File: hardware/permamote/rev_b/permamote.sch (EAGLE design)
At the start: 130 parts, among them J1 TC2030-JLINK-L, J2 M10X2, J3 M04X2, Q1 PMDXB950UPEL, Q10 CSD22206W, Q11 CSD22206W, Q2 PMDXB950UPEL, Q3 PMDXB950UPEL, Q4 PMDXB950UPEL, Q5 PMDXB950UPEL, Q6 PMDXB950UPEL, Q7 CSD22206W, Q8 CSD22206W, Q9 CSD22206W, U1 AB1815-T3, U10 NRF52840, U11 SI7021-A20-GM1, U2 BQ25505, U3 EKMB1101111, U4 ISL29125, U5 LIS2DW12, U6 MAX17222, U7 MAX44009, U8 MS5637-02BA03, U9 NRF51822QF, X1 32MHz, X2 ABS05-32.768KHZ-9-T, X3 32.768kHz, X4 ABS07-32.768KHZ-7-T, X5 16MHz

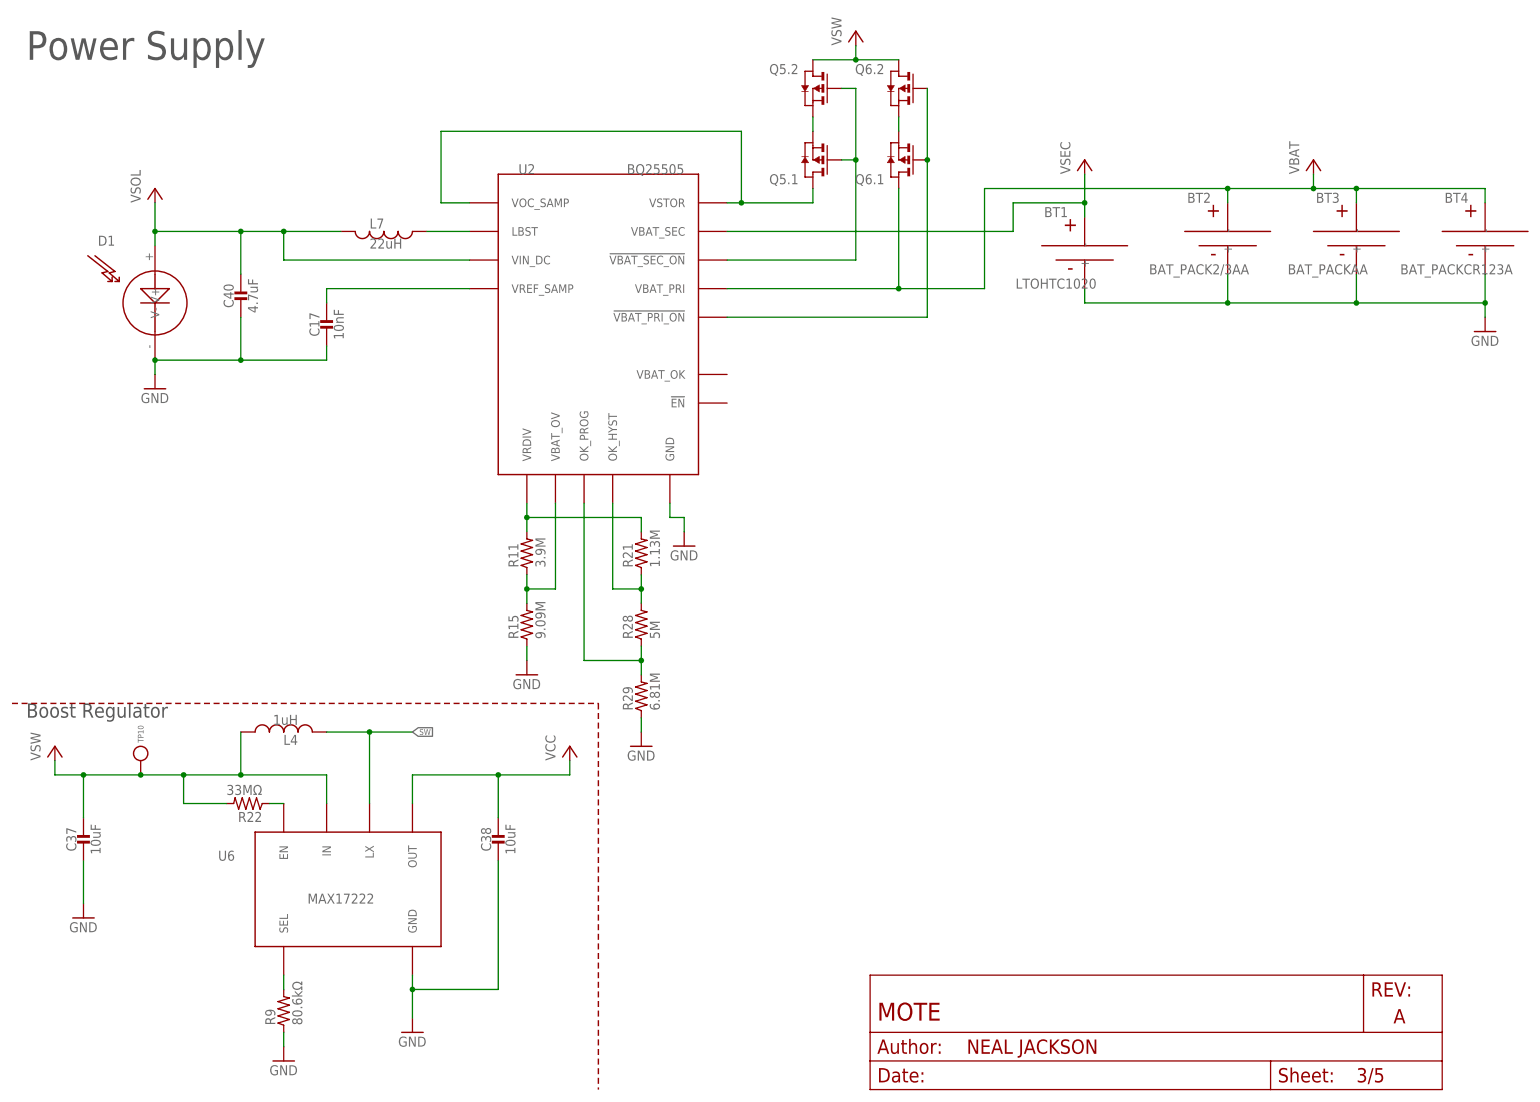
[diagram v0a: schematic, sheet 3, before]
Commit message: fixed bq dividers, changed inductor
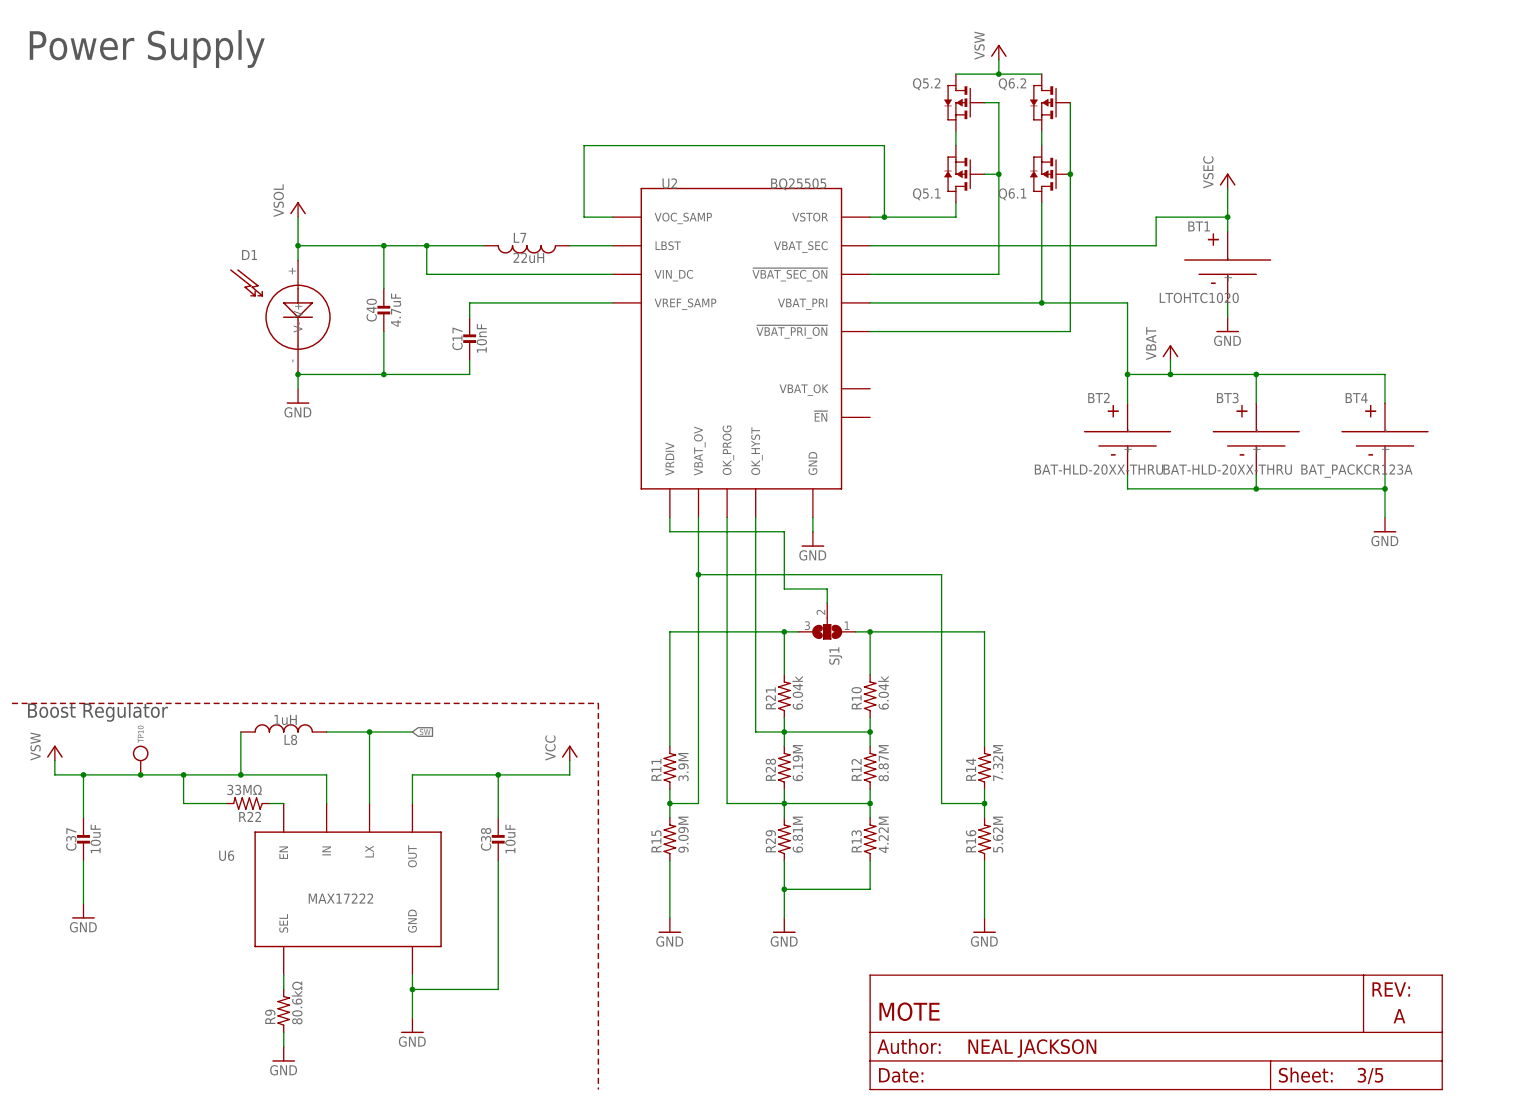
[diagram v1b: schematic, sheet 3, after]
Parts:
- removed L4: 1uH, passives:INDUCTORIHL2525CZ
- added L8: 1uH, passives:INDUCTORIHL
- added R10: 6.04k, passives:RESISTOR0402_RES
- added R12: 8.87M, passives:RESISTOR0402_RES
- added R13: 4.22M, passives:RESISTOR0402_RES
- added R14: 7.32M, passives:RESISTOR0402_RES
- added R16: 5.62M, passives:RESISTOR0402_RES
- added SJ1: (no value), jumper:SJ2W
- BT2: value BAT_PACK2/3AA -> BAT-HLD-20XX-THRU; device batteries:BAT_PACK2/3AA -> batteries:BAT-HLD-20XX-THRU
- BT3: value BAT_PACKAA -> BAT-HLD-20XX-THRU; device batteries:BAT_PACKAA -> batteries:BAT-HLD-20XX-THRU
- R21: value 1.13M -> 6.04k
- R28: value 5M -> 6.19M
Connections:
- new net N$1: R11.2, R21.2, SJ1.3
- new net N$16: R10.2, R14.2, SJ1.1
- net GND: now also R13.1, R16.1
- net N$18: now also R14.1, R16.2
- net N$32: now also SJ1.2; no longer R11.2, R21.2
- net N$57: now also R12.1, R13.2
- net N$58: now also R10.1, R12.2
- net SW: now also L8.2; no longer L4.2
- net VSW: now also L8.1; no longer L4.1
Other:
- note added: "Divider for Lithium Polymer"
- note added: "Divider for Lithium Titanate"
- moved on the sheet: BT1, BT2, BT3, BT4, C17, C40, D1, L7, Q5.1, Q5.2, Q6.1, Q6.2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

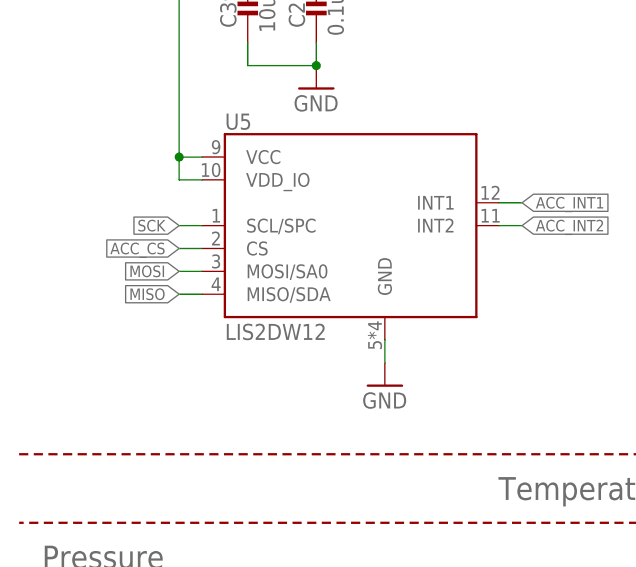
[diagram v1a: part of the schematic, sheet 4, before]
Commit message: Fix miso/mosi switch
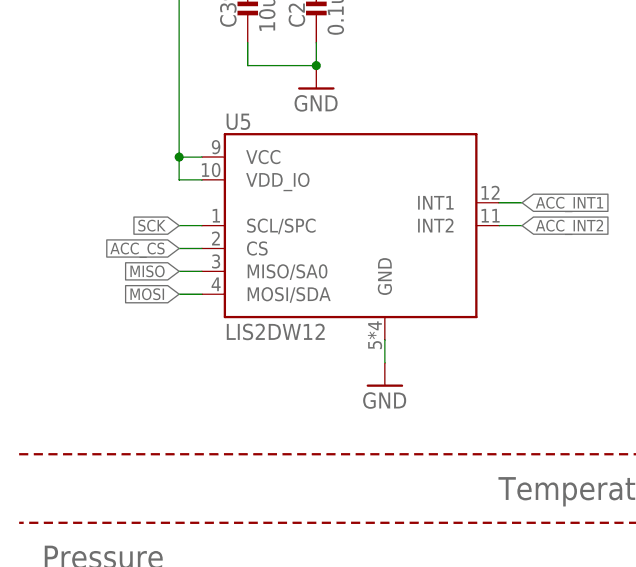
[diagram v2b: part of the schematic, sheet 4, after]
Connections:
- net MISO: now also U5.MISO/SA0; no longer U5.MISO/SDA
- net MOSI: now also U5.MOSI/SDA; no longer U5.MOSI/SA0
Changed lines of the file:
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@@
 <?xml version="1.0" encoding="utf-8"?>
 <!DOCTYPE eagle SYSTEM "eagle.dtd">
-<eagle version="8.4.1">
+<eagle version="8.4.2">
 <drawing>
 <settings>
@@
 <setting verticaltext="up"/>
 </settings>
-<grid distance="0.1" unitdist="inch" unit="inch" style="lines" multiple="1" display="yes" altdistance="0.05" altunitdist="inch" altunit="inch"/>
+<grid distance="0.1" unitdist="inch" unit="inch" style="lines" multiple="1" display="no" altdistance="0.01" altunitdist="inch" altunit="inch"/>
 <layers>
 <layer number="1" name="Top" color="4" fill="1" visible="no" active="no"/>
@@
 <segment>
 <pinref part="U2" gate="G$1" pin="VRDIV"/>
-<wire x1="116.84" y1="101.6" x2="116.84" y2="99.06" width="0.1524" layer="91"/>
-<wire x1="137.16" y1="99.06" x2="116.84" y2="99.06" width="0.1524" layer="91"/>
-<wire x1="137.16" y1="99.06" x2="137.16" y2="88.9" width="0.1524" layer="91"/>
-<wire x1="137.16" y1="88.9" x2="144.78" y2="88.9" width="0.1524" layer="91"/>
+<wire x1="116.84" y1="88.9" x2="116.84" y2="101.6" width="0.1524" layer="91"/>
+<wire x1="116.84" y1="88.9" x2="144.78" y2="88.9" width="0.1524" layer="91"/>
 <pinref part="SJ1" gate="G$1" pin="2"/>
 <wire x1="144.78" y1="88.9" x2="144.78" y2="86.36" width="0.1524" layer="91"/>
@@
 </segment>
 </net>
-<net name="MOSI" class="0">
-<segment>
-<pinref part="U5" gate="G$1" pin="MOSI/SA0"/>
-<wire x1="20.32" y1="109.22" x2="17.78" y2="109.22" width="0.1524" layer="91"/>
-<label x="17.78" y="109.22" size="1.27" layer="95" rot="R180" xref="yes"/>
-</segment>
-</net>
-<net name="MISO" class="0">
-<segment>
-<pinref part="U5" gate="G$1" pin="MISO/SDA"/>
-<wire x1="20.32" y1="106.68" x2="17.78" y2="106.68" width="0.1524" layer="91"/>
-<label x="17.78" y="106.68" size="1.27" layer="95" rot="R180" xref="yes"/>
-</segment>
-</net>
 <net name="ACC_INT1" class="0">
 <segment>
@@
 </segment>
 </net>
+<net name="MISO" class="0">
+<segment>
+<pinref part="U5" gate="G$1" pin="MISO/SA0"/>
+<wire x1="20.32" y1="109.22" x2="17.78" y2="109.22" width="0.1524" layer="91"/>
+<label x="17.78" y="109.22" size="1.27" layer="95" rot="R180" xref="yes"/>
+</segment>
+</net>
+<net name="MOSI" class="0">
+<segment>
+<pinref part="U5" gate="G$1" pin="MOSI/SDA"/>
+<wire x1="20.32" y1="106.68" x2="17.78" y2="106.68" width="0.1524" layer="91"/>
+<label x="17.78" y="106.68" size="1.27" layer="95" rot="R180" xref="yes"/>
+</segment>
+</net>

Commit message: WIP rev_b
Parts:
- removed A1: ANT3216A063R2400A, chips:ANT3216A063R2400A
- removed B2: BAL-NRF01D3, chips:BAL-NRF01D3
- removed C14, C15: 1nF, passives:CAPACITOR0402_CAP
- removed C16: 2.2nF, passives:CAPACITOR0402_CAP
- removed C19: 47nF, passives:CAPACITOR0402_CAP
- removed C28: 0.1uF, passives:CAPACITOR0402_CAP
- removed C3: 0.8pF, passives:CAPACITOR0402_CAP
- removed C34: 1uF, passives:CAPACITOR0402_CAP
- removed C36: 4.7uF, passives:CAPACITOR0402_CAP
- removed C6, C7, C8, C9: 12pF, passives:CAPACITOR0402_CAP
- removed H1, H2, H3, H4: MOUNT-PAD-ROUND3.0, holes:MOUNT-PAD-ROUND3.0
- removed JP1, JP2, JP3, JP4, JP5, JP6, JP7, JP8: (no value), SparkFun-Passives:JUMPER-2SMD-NC
- removed JP10, JP11, JP12, JP13, JP14, JP15, JP16, JP9: (no value), SparkFun-Connectors:M02PTH
- removed L2: 15nH, passives:INDUCTOR0402
- removed L5: 10uH, passives:INDUCTOR0603
- removed Q11, Q9: CSD22206W, fets:CSD22206W
- removed R8: 12kΩ, passives:RESISTOR0402_RES
- removed TP10: TEST_POINT_0.040IN, headers:TEST_POINT_0.040IN
- removed U9: NRF51822QF, chips:NRF51822QF
- removed X2: ABS05-32.768KHZ-9-T, crystals:ABS05-32.768KHZ-9-T
- removed X5: 16MHz, crystals:TXC-8Y
- added C41: 0.1uF, passives:CAPACITOR0402_CAP
- added J5: MICRO_USB_B_HIROSE_ZX62R-B-5P, connector:MICRO_USB_B_HIROSE_ZX62R-B-5P
- added U12: FT232RQ, ftdichip:FT232RQ
- J1: value TC2030-JLINK-L -> TC2030-JLINK-NL; device connector:TC2030-JLINK-L -> connector:TC2030-JLINK-NL
- Q10, Q7, Q8: value CSD22206W -> PMDXB950UPEL; device fets:CSD22206W -> fets:PMDXB950UPEL
- R1: value 150Ω -> 10kΩ; DIGIKEY 311-150JRCT-ND -> 311-10KJRCT-ND
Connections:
- removed net AVDD1: C14.1, C34.1, L2.1, U9.AVDD
- removed net DCC1: L5.2, U9.DCC
- removed net N$15: C25.1, C39.1, JP1.1, JP11.1, U5.VCC, U5.VDD_IO
- removed net N$19: C26.1, JP15.1, JP4.1, Q9.S, R25.2
- removed net N$24: JP14.1, JP8.1, Q11.S, R27.2
- removed net N$33: C24.1, C31.1, JP12.1, JP2.1, Q7.S, R23.2, R4.2
- removed net N$36: C27.1, JP16.1, JP5.1, Q10.S, R26.2
- removed net N$37: C32.1, JP13.1, JP3.1, Q8.S, R24.2, R5.2
- removed net N$42: C33.1, JP10.1, JP6.1, U1.VCC
- removed net N$60: B2.ANT1, U9.ANT1
- removed net N$61: B2.ANT2, U9.ANT2
- removed net N$62: A1.ANTENNA, B2.SE, C3.1
- removed net N$63: L2.2, L5.1
- removed net N$64: C6.1, U9.XC1, X5.1
- removed net N$65: C7.1, U9.XC2, X5.2
- removed net N$66: C15.1, U9.DEC1
- removed net N$67: C19.1, U9.DEC2
- removed net NRF_A2: C9.1, U9.P27/AIN1/XL1, X2.2
- removed net NRF_A3: C8.1, U9.P26/AIN0/XL2, X2.1
- removed net VCC_JUMP: C20.1, C21.1, C23.1, C28.1, C29.1, C35.1, C36.1, JP7.1, JP9.1, U10.VDD, U10.VDDH, U9.VDD
- removed net VDD_PA1: B2.VDD_PA, C16.1, U9.VDD_PA
- new net D+: J5.D+, U12.USBDP
- new net D-: J5.D-, U12.USBDM
- new net DBG_RX: U12.TXD
- new net DBG_TX: U12.RXD
- new net N$13: C41.1, U12.3V3OUT
- new net USB_5V: J5.+5V, U12.VCC
- net !ACC_EN: no longer U10.P1.15, U9.P16
- net !CLR_EN: now also Q7.1.G; no longer Q7.G, U9.P17
- net !CLR_INT: no longer U9.P29
- net !HUM_EN: now also Q8.2.G; no longer Q10.G, U9.P15
- net !LT_EN: now also Q7.2.G; no longer Q8.G, U9.P18
- net !LT_INT: no longer U9.P28
- net !PIR_EN: now also Q10.1.G; no longer Q11.G, U9.P19
- net !PR_EN: now also Q8.1.G; no longer Q9.G, U9.P20
- net !RST: now also U12.!RESET; no longer R1.1
- net !RTC_IRQ1: no longer U9.P25
- net !RTC_IRQ2: no longer U9.P24
- net !RTC_IRQ3: no longer U9.P23
- net ACC_CS: no longer U9.P14
- net ACC_INT1: no longer U9.P06/AIN7/AREF1
- net ACC_INT2: no longer U9.P07
- net GND: now also C41.2, J5.GND, U12.GND, U12.GND@1, U12.GND@2, U12.GND@A, U12.TEST; no longer A1.GND, B2.GND, C14.2, C15.2, C16.2, C19.2, C28.2, C3.2, C34.2, C36.2, C6.2, C7.2, C8.2, C9.2, H1.MOUNT, H2.MOUNT, H3.MOUNT, H4.MOUNT, R8.2, U9.GND
- net MISO: no longer U9.P11
- net MOSI: no longer U9.P12
- net N$20: now also Q7.2.D; no longer Q8.D
- net N$21: now also Q8.1.D; no longer Q9.D
- net N$22: now also Q8.2.D; no longer Q10.D
- net N$23: now also Q10.1.D; no longer Q11.D
- net N$31: now also Q7.1.D; no longer Q7.D
- net PIR_OUT: no longer U9.P30
- net RTC_CS: no longer U9.P22
- net SCK: no longer U9.P13
- net SCL: no longer U9.P10
- net SDA: no longer U9.P08
- net SW: no longer U9.P04/AIN5
- net SWDCLK: no longer R8.1, U9.SWDCLK
- net SWDIO: no longer J1.SWO, R1.2, U9.SWDIO/!RESET
- net VBAT: now also U1.VBAT; no longer JP10.2, JP6.2, R6.2, R7.2, U9.P02/AIN3
- net VCC: now also C20.1, C21.1, C23.1, C24.1, C25.1, C26.1, C27.1, C29.1, C31.1, C32.1, C33.1, C35.1, C39.1, Q10.1.S, Q7.1.S, Q7.2.S, Q8.1.S, Q8.2.S, R1.2, R23.2, R24.2, R25.2, R26.2, R27.2, R4.2, R5.2, R6.2, R7.2, U1.VCC, U10.VDD, U10.VDDH, U12.VCCIO, U5.VCC, U5.VDD_IO; no longer JP1.2, JP11.2, JP12.2, JP13.2, JP14.2, JP15.2, JP16.2, JP2.2, JP3.2, JP4.2, JP5.2, JP7.2, JP8.2, JP9.2
- net VSEC: no longer U9.P01/AIN2
- net VSOL: no longer U9.P03/AIN4
- net VSW: no longer TP10.TESTPOINT
- net WDI: now also R1.1; no longer U9.P21
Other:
- note added: "Debugging"
- note removed: "Auxillary NRF51822"
- note removed: "Mounting Holes"

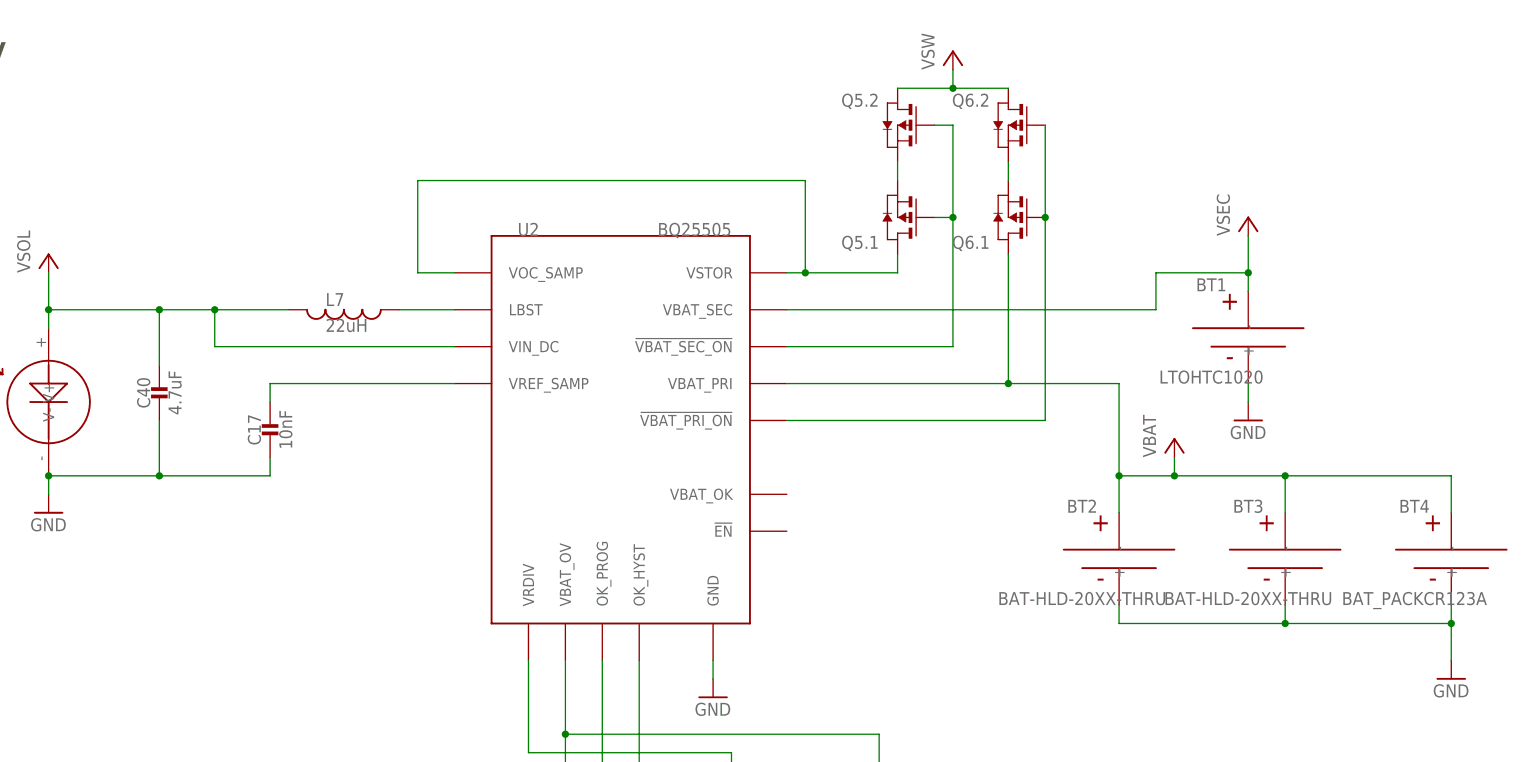
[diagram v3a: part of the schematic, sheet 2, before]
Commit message: WIP
Finish power routing
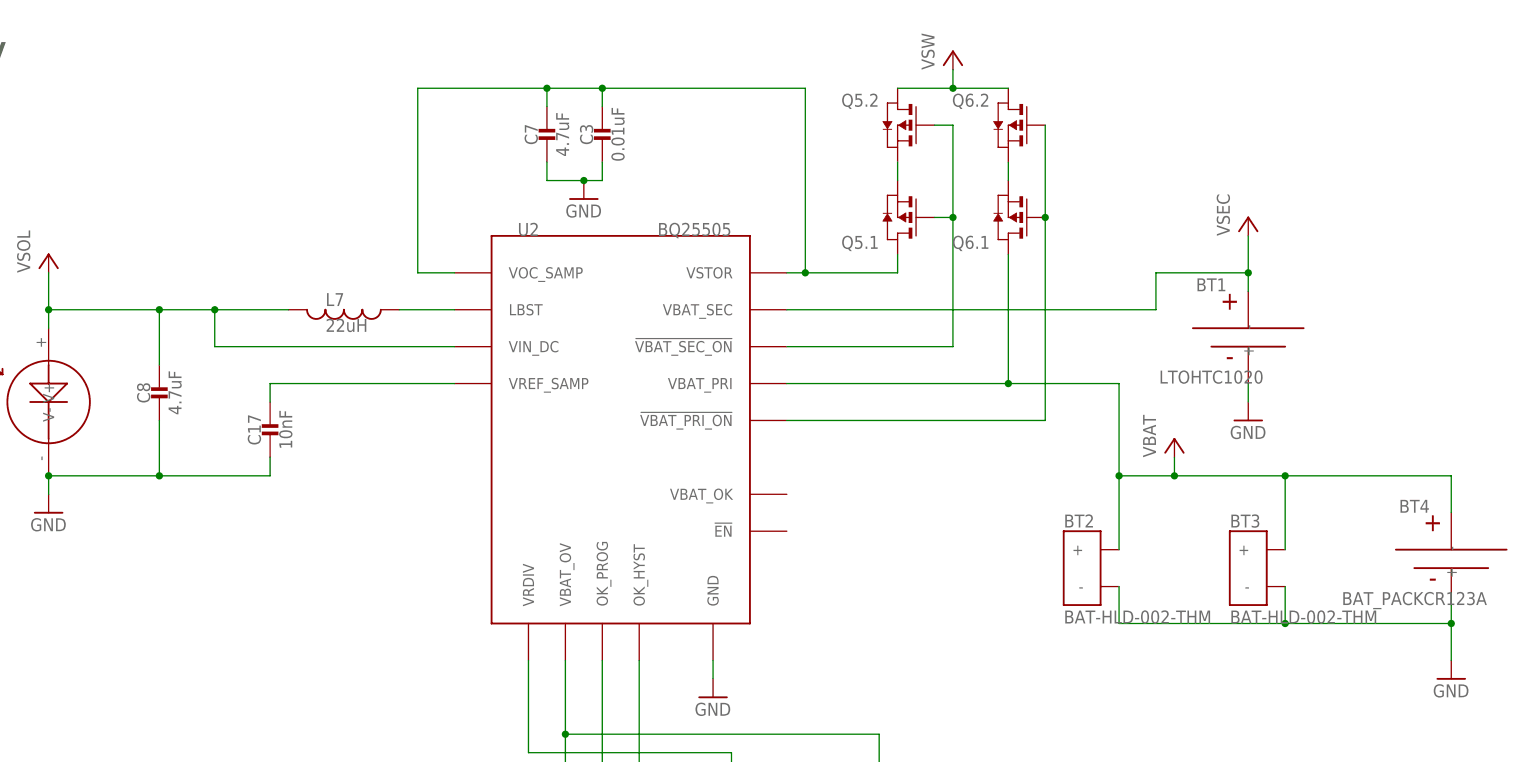
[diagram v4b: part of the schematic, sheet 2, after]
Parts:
- removed C40: 4.7uF, passives:CAPACITOR0603_CAP
- added C3: 0.01uF, passives:CAPACITOR0402_CAP
- added C7, C8: 4.7uF, passives:CAPACITOR0402_CAP
- BT2, BT3: value BAT-HLD-20XX-THRU -> BAT-HLD-002-THM; device batteries:BAT-HLD-20XX-THRU -> batteries:BAT-HLD-002-THM
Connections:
- net N$30 renamed VREF_SAMP
- net N$40 renamed LBST
- net N$46 renamed !VBAT_SEC_ON
- net N$56 renamed !VBAT_PRI_ON
- removed net N$47: Q5.1.D, U2.VOC_SAMP, U2.VSTOR
- new net VOC_SAMP_VSTOR: C3.1, C7.1, Q5.1.D, U2.VOC_SAMP, U2.VSTOR
- net GND: now also C3.2, C7.2, C8.2; no longer C40.2
- net VSOL: now also C8.1; no longer C40.1
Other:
- moved on the sheet: BT2, BT3
